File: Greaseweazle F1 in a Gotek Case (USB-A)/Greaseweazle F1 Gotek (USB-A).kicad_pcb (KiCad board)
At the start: 2 copper layers, 111.6 x 68.1 mm, 58 parts, among them CN1 Floppy Data, J1 PinHeader_1x04_P2.54mm_Vertic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, J1 USB A, J2 Floppy Power, J3 Programming Port, SW1 Reset, U1 Blue Pill

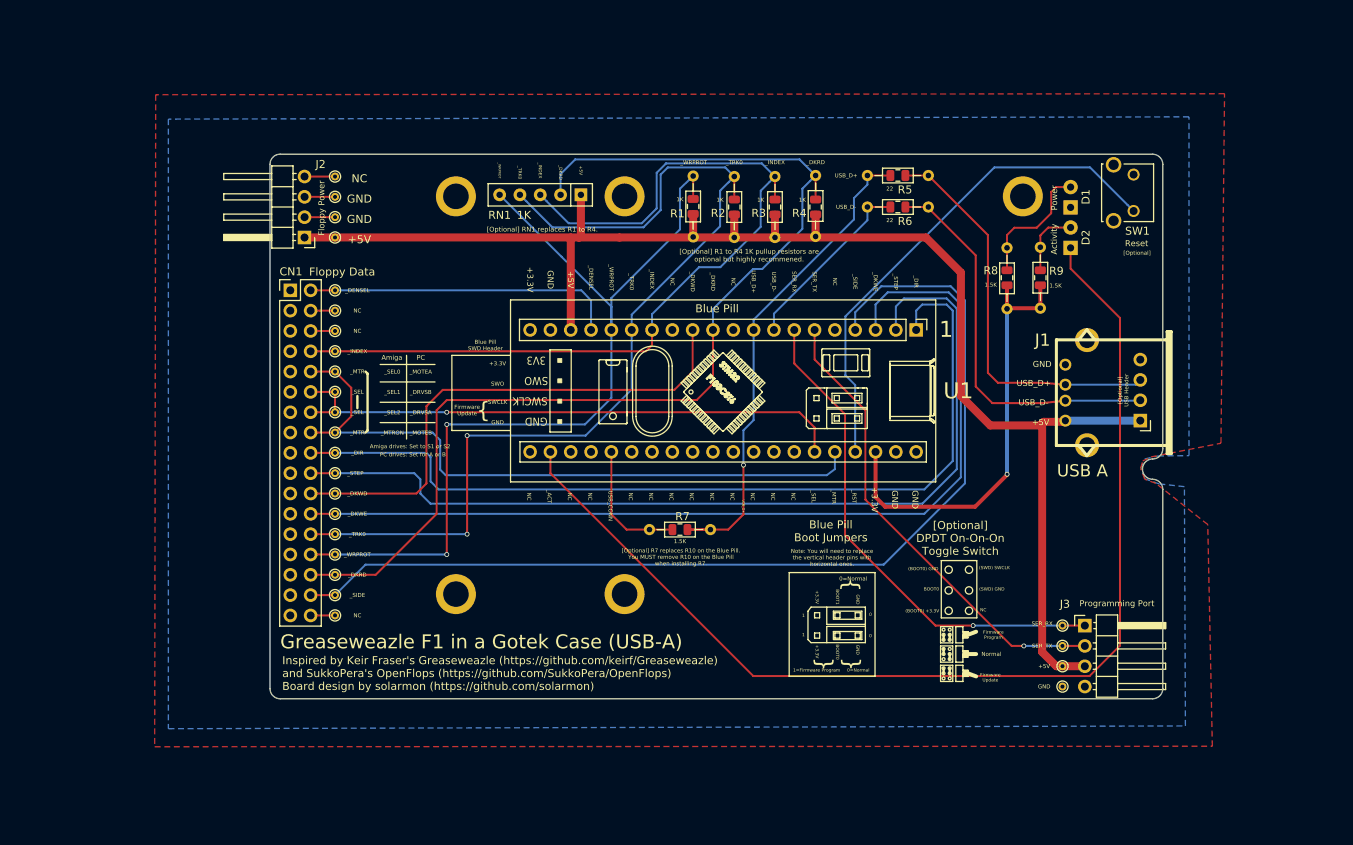
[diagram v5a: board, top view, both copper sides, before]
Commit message: Tweaks after first build test
* Increased size of silk screen text
* Moved notch down a bit
* Swap +5V and GND on Programming port
* Moved LED holes nearer towards front.
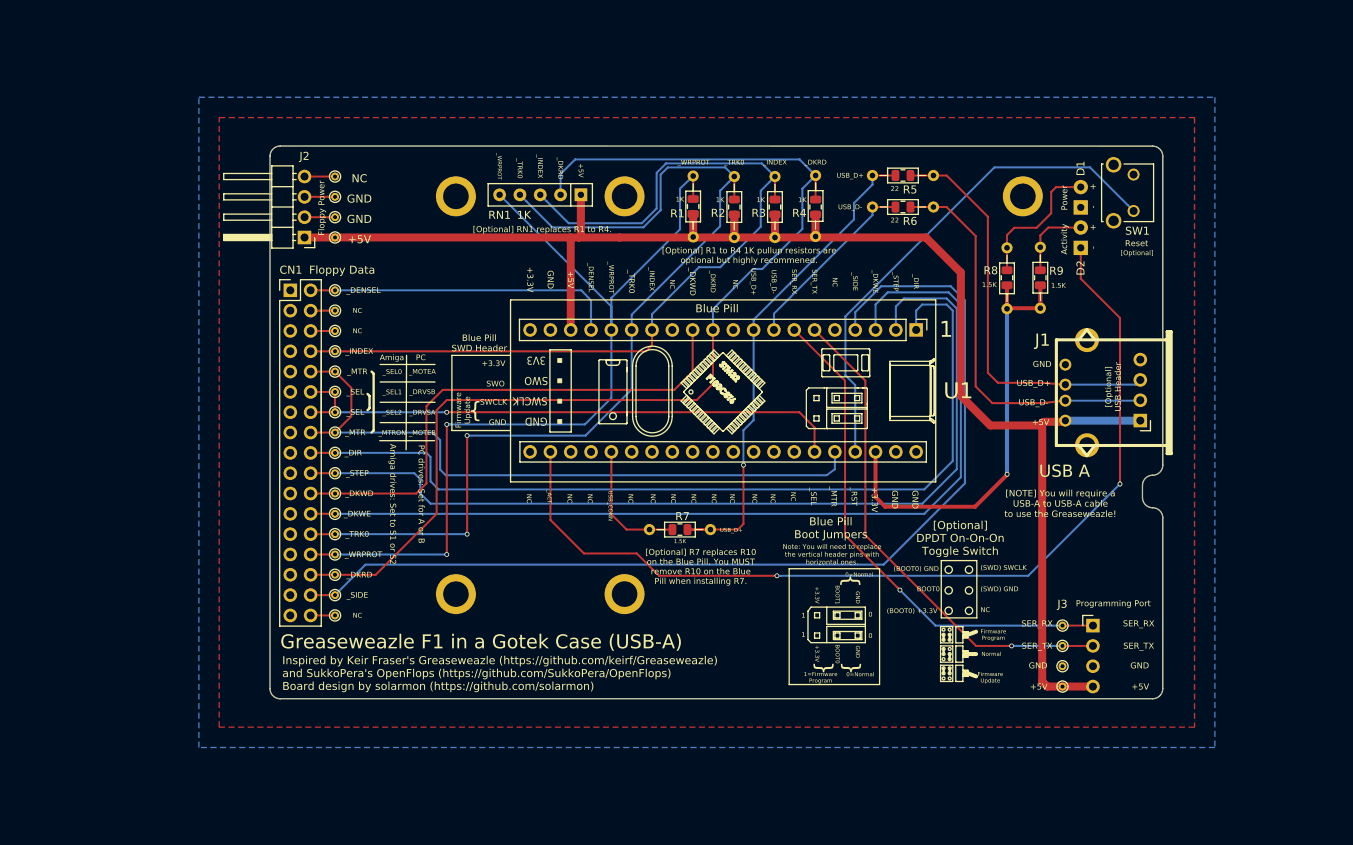
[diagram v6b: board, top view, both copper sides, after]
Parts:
- moved D1 1.27 mm to (196.6, 62.0)
- moved D2 1.27 mm to (196.6, 67.1)
- moved J3 1.02 mm to (198.1, 114.3)
- moved R5 0.64 mm to (178.2, 58.0)
- moved R5 0.64 mm to (174.4, 58.0)
- moved R6 0.64 mm to (178.2, 62.0)
- moved R6 0.64 mm to (174.4, 62.0)
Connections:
- ? pad 1: +5V -> GND
- ? pad 1: GND -> +5V
- J3 pad 3: +5V -> GND
- J3 pad 4: GND -> +5V
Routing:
- net /_ACT: track 138.2 -> 119.1 mm, vias 0 -> 2
- net +5V: track 186.5 -> 190.8 mm
- net /SER_TX: track 58.8 -> 62.5 mm
- net Net-(D2-Pad2): track 8.54 -> 9.81 mm
- net Net-(D1-Pad2): track 16.4 -> 17.7 mm
- net /SER_RX: track 62.9 -> 64.0 mm
- net /USB_D+: track 62.5 -> 63.5 mm
- net Net-(J1-Pad3): track 50.4 -> 51.1 mm
- net Net-(J1-Pad2): track 49.3 -> 49.9 mm
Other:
- board size 111.6 x 68.1 mm -> 111.6 x 69.1 mm
- board text added: "+"
- board text added: "-"
- board text added: "[NOTE] You will require a USB-A to USB-A cable to use the Greaseweazle!"
